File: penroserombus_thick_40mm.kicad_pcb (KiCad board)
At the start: 2 copper layers, 52.4 x 38 mm, 15 parts, among them J1 Conn_01x03_Female, J2 Conn_01x03_Female, J3 Conn_01x03_Male, J4 Conn_01x03_Male, M2 MountingHole_2.2mm_M2_ISO7380, SW1 SW_DPDT_x2

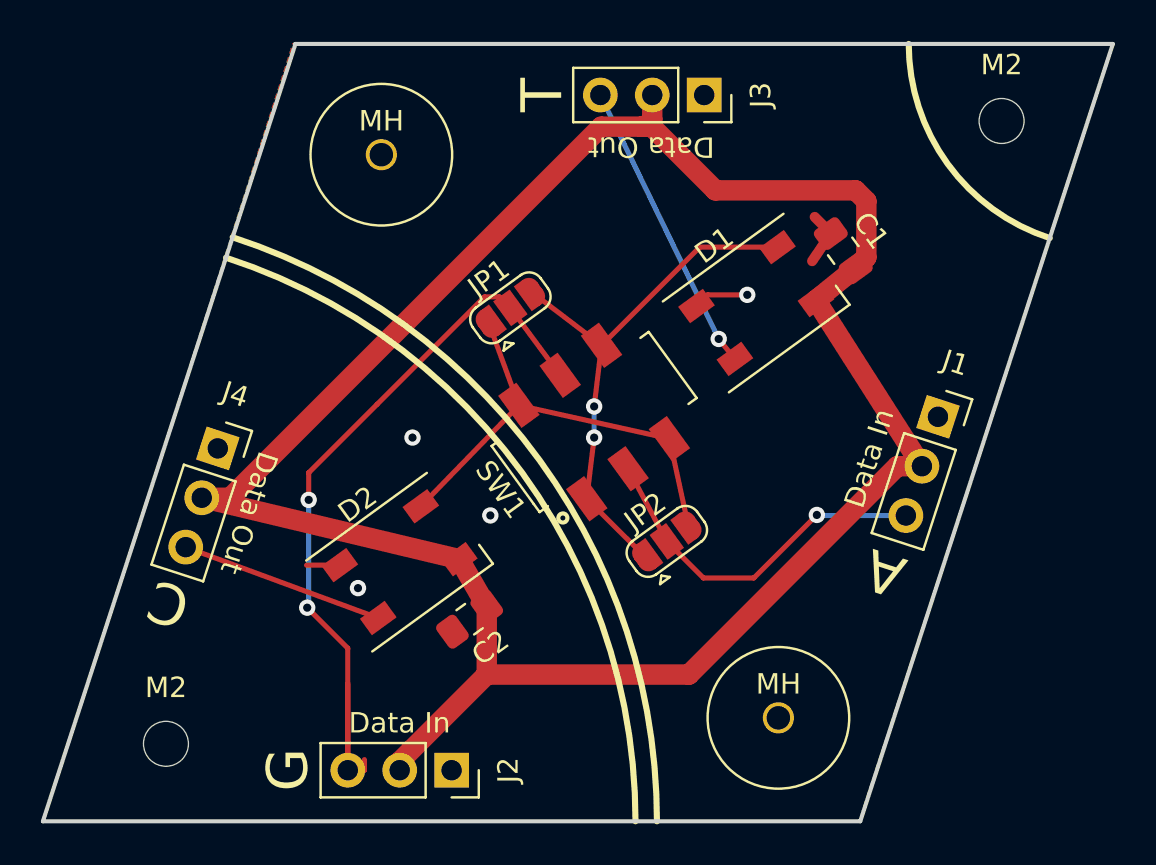
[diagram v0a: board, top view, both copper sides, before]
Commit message: made 3535 led version
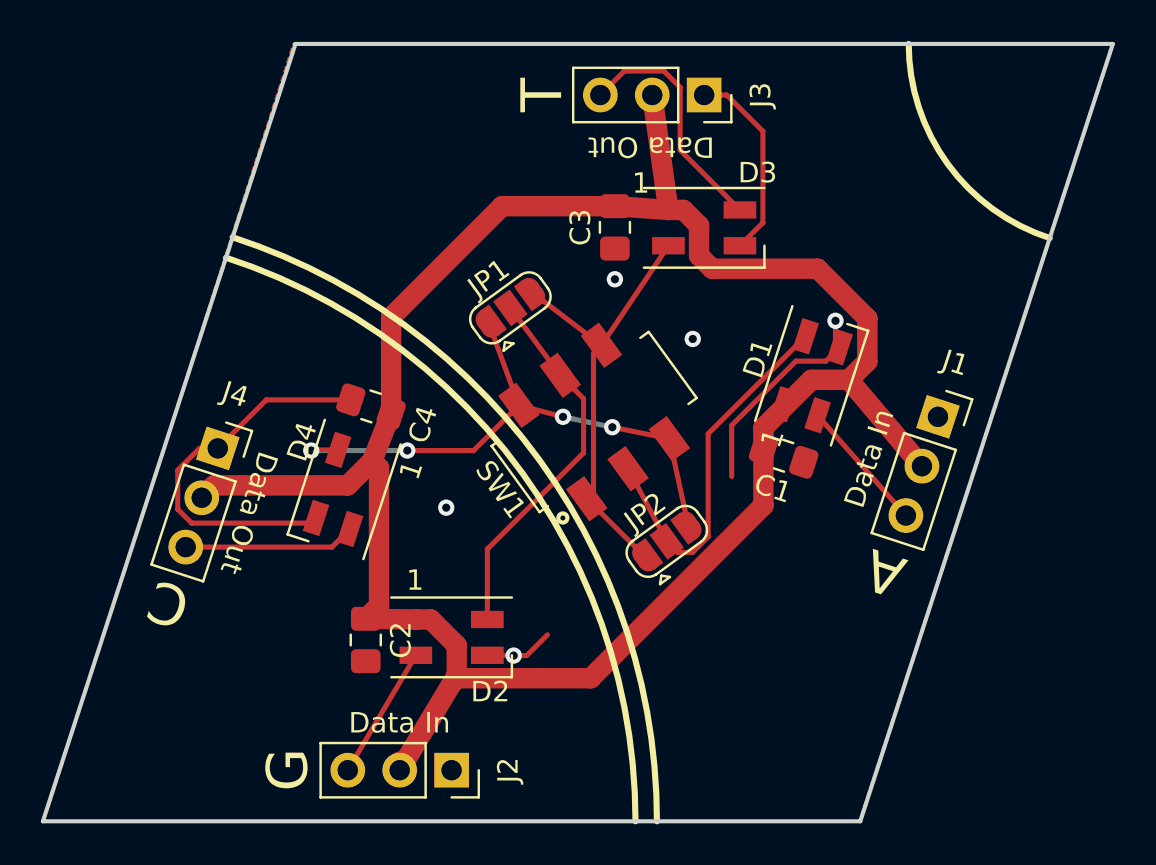
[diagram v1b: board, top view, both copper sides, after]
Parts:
- removed M2 (x2): MountingHole_2.2mm_M2_ISO7380, MountingHole:MountingHole_2.2mm_M2_ISO7380
- removed MH (x2): Pushpin_mountinghole, penroserombus:Pushpin_mountinghole
- added C3: C, Capacitor_SMD:C_0805_2012Metric_Pad1.18x1.45mm_HandSolder, F.Cu at (148.8, 85.0)
- added C4: C, Capacitor_SMD:C_0805_2012Metric_Pad1.18x1.45mm_HandSolder, F.Cu at (136.9, 93.7)
- added D3: SK6812, LED_SMD:LED_SK6812MINI_PLCC4_3.5x3.5mm_P1.75mm, F.Cu at (153.2, 85.0)
- added D4: SK6812, LED_SMD:LED_SK6812MINI_PLCC4_3.5x3.5mm_P1.75mm, F.Cu at (135.6, 97.8)
- D1, D2: footprint LED_SMD:LED_SK6812_PLCC4_5.0x5.0mm_P3.2mm -> LED_SMD:LED_SK6812MINI_PLCC4_3.5x3.5mm_P1.75mm
- moved C1 10.4 mm to (157.1, 96.1), turned to 162 degrees
- moved C2 5.18 mm to (136.7, 105.2), turned to 90 degrees
- moved D1 4.48 mm to (158.5, 92.2), turned to 72 degrees
- moved D2 4.48 mm to (140.9, 105.0), turned to 0 degrees
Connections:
- J1 pad 3: Net-(J1-Pad3) -> Net-(D1-Pad2)
- J2 pad 3: Net-(J2-Pad3) -> Net-(D2-Pad2)
- J3 pad 3: Net-(D1-Pad4) -> Net-(D3-Pad4)
- J4 pad 3: Net-(D2-Pad4) -> Net-(D4-Pad4)
- JP1 pad 1: Net-(D2-Pad2) -> Net-(D4-Pad2)
- JP1 pad 2: Net-(J2-Pad3) -> Net-(D2-Pad4)
- JP1 pad 3: Net-(D1-Pad2) -> Net-(D3-Pad2)
- JP2 pad 1: Net-(D1-Pad2) -> Net-(D3-Pad2)
- JP2 pad 2: Net-(J1-Pad3) -> Net-(D1-Pad4)
- JP2 pad 3: Net-(D2-Pad2) -> Net-(D4-Pad2)
- SW1 pad 1: Net-(D1-Pad2) -> Net-(D3-Pad2)
- SW1 pad 2: Net-(J1-Pad3) -> Net-(D1-Pad4)
- SW1 pad 3: Net-(D2-Pad2) -> Net-(D4-Pad2)
- SW1 pad 4: Net-(D2-Pad2) -> Net-(D4-Pad2)
- SW1 pad 5: Net-(J2-Pad3) -> Net-(D2-Pad4)
- SW1 pad 6: Net-(D1-Pad2) -> Net-(D3-Pad2)
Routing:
- net Net-(J2-Pad3): track 39.3 -> 0.00 mm, vias 2 -> 0
- net GND: track 6.94 -> 42.8 mm, vias 4 -> 5
- net Net-(D4-Pad2): track 0.00 -> 28.6 mm, vias 0 -> 4
- net Net-(D3-Pad2): track 0.00 -> 22.0 mm
- net Net-(D1-Pad2): track 26.5 -> 6.54 mm, vias 2 -> 0
- net Net-(J1-Pad3): track 17.8 -> 0.00 mm, vias 1 -> 0
- net Net-(D2-Pad2): track 23.1 -> 6.54 mm
- net Net-(D3-Pad4): track 0.00 -> 11.9 mm
- net Net-(D2-Pad4): track 10.0 -> 18.5 mm
- net Net-(D4-Pad4): track 0.00 -> 8.41 mm
- net Net-(D1-Pad4): track 14.5 -> 18.4 mm, vias 1 -> 0
- net VCC: track 110.0 -> 107.4 mm

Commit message: added mounting holes
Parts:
- added MH: Pushpin_mountinghole, penroserombus:Pushpin_mountinghole, F.Cu at (156.2, 108.1)
- added MH: Pushpin_mountinghole, penroserombus:Pushpin_mountinghole, F.Cu at (137.0, 81.2)
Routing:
- net GND: track 42.8 -> 43.8 mm, vias 5 -> 4

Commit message: updated thick rombus
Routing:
- net GND: track 43.8 -> 35.4 mm, vias 4 -> 9
- net Net-(D4-Pad2): track 28.6 -> 26.6 mm
